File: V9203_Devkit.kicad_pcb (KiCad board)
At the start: 2 copper layers, 50 x 50 mm, 101 parts, among them J1 RJ45, J10 GS3, J2 CONN_01X16, J3 CONN_01X12, J4 Screw_Terminal_1x04, J5 GROVE-CONNECTOR-SMD-90D(4+2P-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, J6 CONN_01X09, J7 GS3, J8 GS3, J9 CONN_01X06, U1 V9203, U2 ROF-78E, Y1 Crystal_GND24

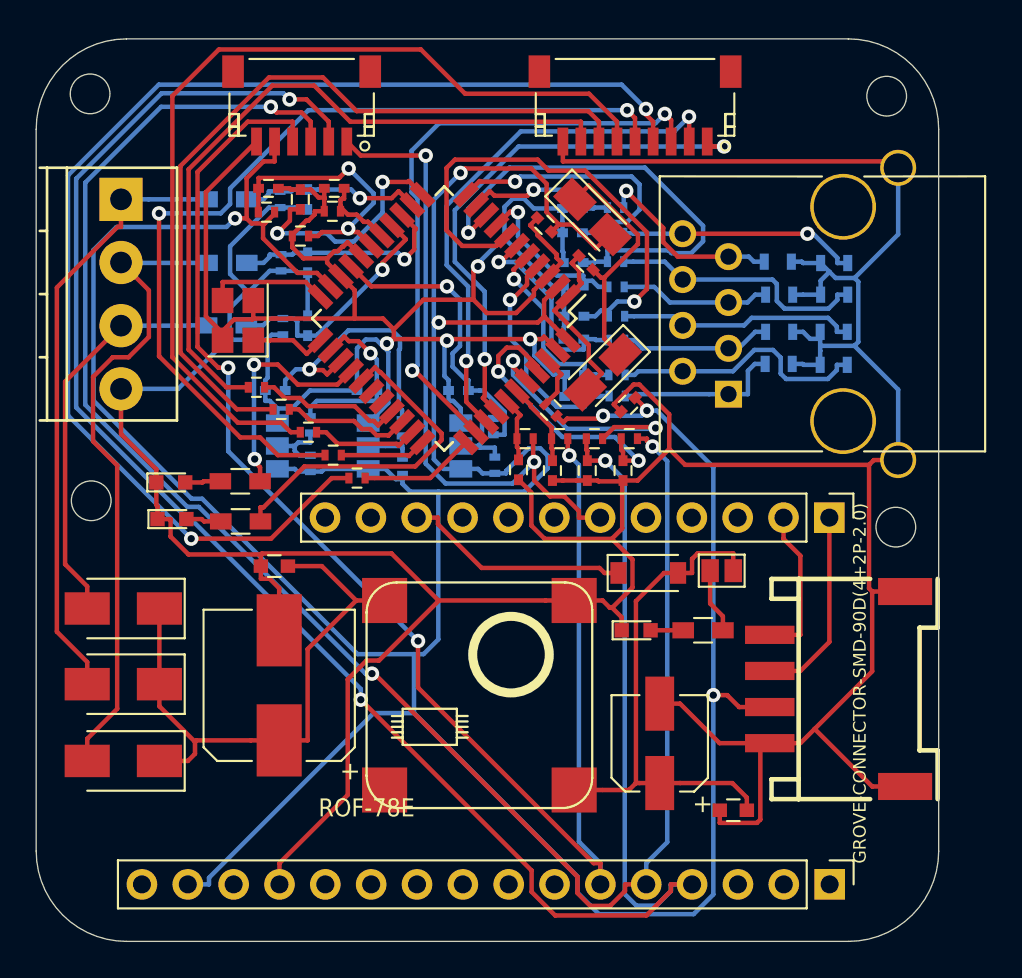
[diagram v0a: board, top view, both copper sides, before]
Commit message: With CS mux, improve silk screen in next rev
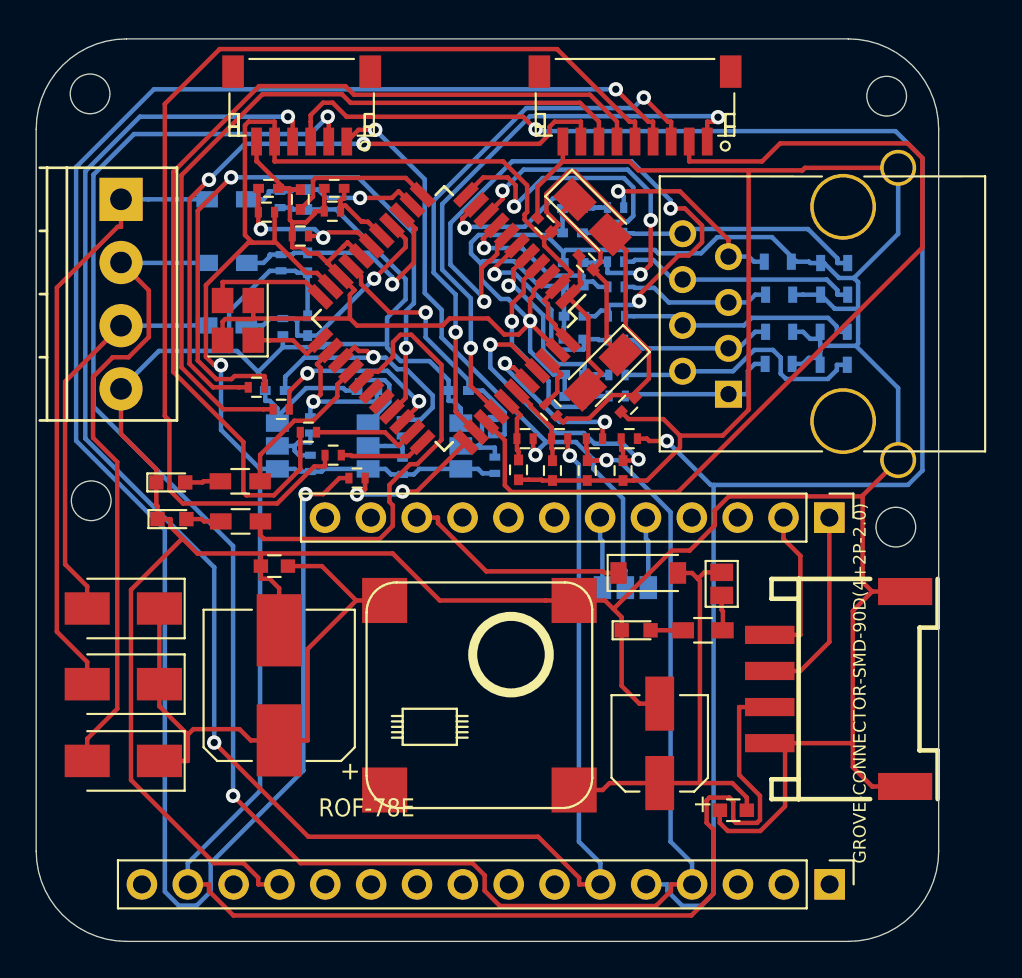
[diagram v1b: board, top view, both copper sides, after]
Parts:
- added J11: GS3, Connect:GS3, B.Cu at (142.6, 70.4)
- moved JP1 0.73 mm to (148.0, 70.2), turned to 180 degrees
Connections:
- J3 pad 6: CS -> Net-(J11-Pad1)
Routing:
- net Net-(J6-Pad4): track 69.7 -> 107.9 mm
- net +3V3: track 207.8 -> 170.5 mm, vias 6 -> 1
- net Net-(R36-Pad1): track 8.25 -> 37.5 mm, vias 0 -> 2
- net GND: track 339.4 -> 363.3 mm, vias 4 -> 1
- net Net-(J6-Pad2): track 29.8 -> 52.6 mm, vias 2 -> 0
- net SCK: track 82.2 -> 98.9 mm
- net Net-(J6-Pad5): track 50.1 -> 62.0 mm, vias 2 -> 0
- net /V9203/IBP: track 27.9 -> 36.4 mm, vias 1 -> 3
- net /V9203/ICP: track 26.5 -> 19.6 mm, vias 1 -> 3
- net Net-(R27-Pad2): track 19.0 -> 25.6 mm
- net Net-(C22-Pad2): track 15.7 -> 9.94 mm
- net /V9203/V_MISO: track 14.6 -> 9.62 mm
- net Net-(C20-Pad2): track 13.1 -> 8.40 mm, vias 2 -> 0
- net Net-(R28-Pad2): track 12.8 -> 8.82 mm, vias 2 -> 0
- net Net-(J11-Pad3): track 0.00 -> 3.93 mm
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
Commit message: Added ground plane
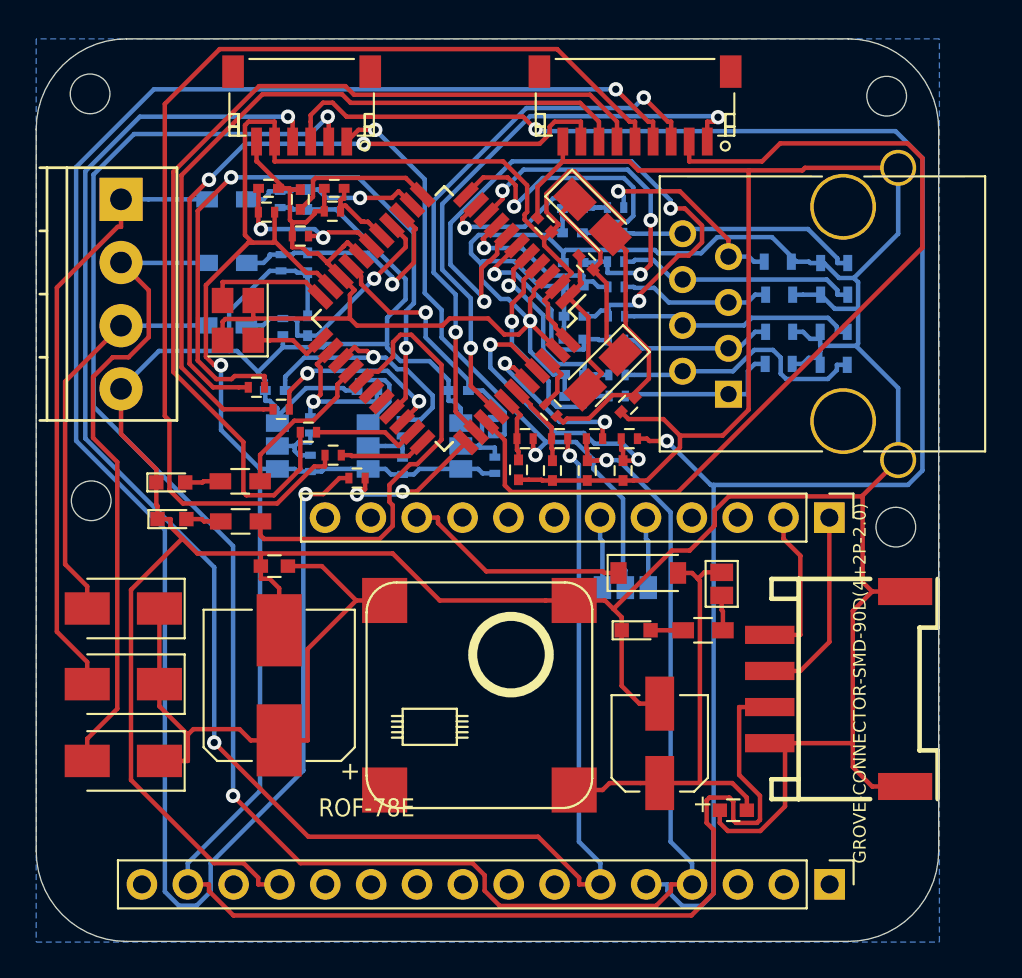
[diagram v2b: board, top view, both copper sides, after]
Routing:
- added copper zone on B.Cu, net GND
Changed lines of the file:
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@@
-(kicad_pcb (version 20170123) (host pcbnew "(2017-03-07 revision cf373e543)-makepkg")
+(kicad_pcb (version 20170123) (host pcbnew "(2017-02-28 revision fd4e2b042)-makepkg")
   (general
     (links 198)
@@
   (segment (start 143.783 67.6979) (end 143.91 67.8249) (width 0.25) (layer B.Cu) (net 93))
   (segment (start 143.783 66.5226) (end 143.783 67.6979) (width 0.25) (layer B.Cu) (net 93))
+  (zone (net 33) (net_name GND) (layer B.Cu) (hatch edge 0.508)
+    (connect_pads (clearance 0.508))
+    (min_thickness 0.254)
+    (fill yes (arc_segments 16) (thermal_gap 0.508) (thermal_bridge_width 0.508))
+    (polygon
+      (pts
+        (xy 110.001429 39.998355) (xy 110.001429 90.036355) (xy 160.039429 90.036355) (xy 160.039429 39.998355)
+      )
+    )
+  )
 )

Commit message: Added silk screen markers
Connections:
- net Net-(C28-Pad1) renamed PM1
- net Net-(C29-Pad1) renamed PM0
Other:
- board text added: "CSMUX"
- board text added: "DSLEEP"
- board text added: "PM0"
- board text added: "PM1"

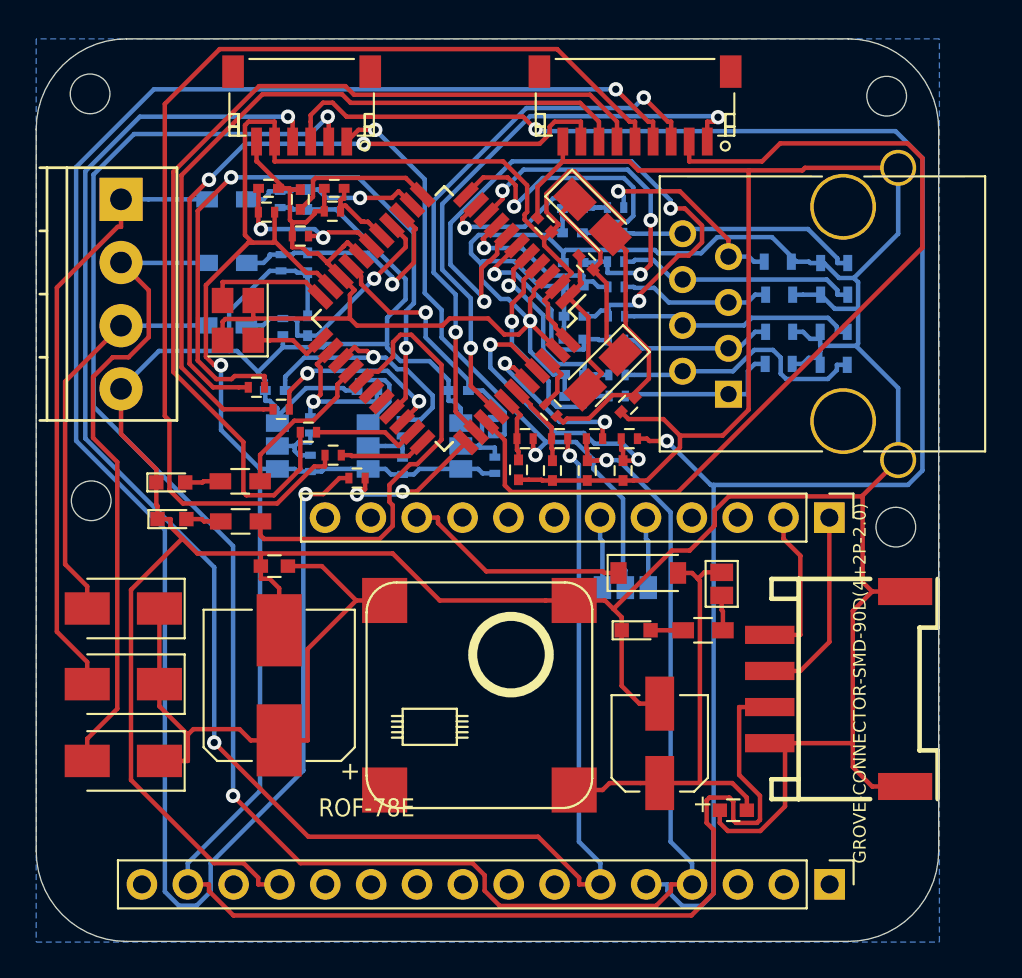
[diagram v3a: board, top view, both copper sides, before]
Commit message: Added silk screen for pins
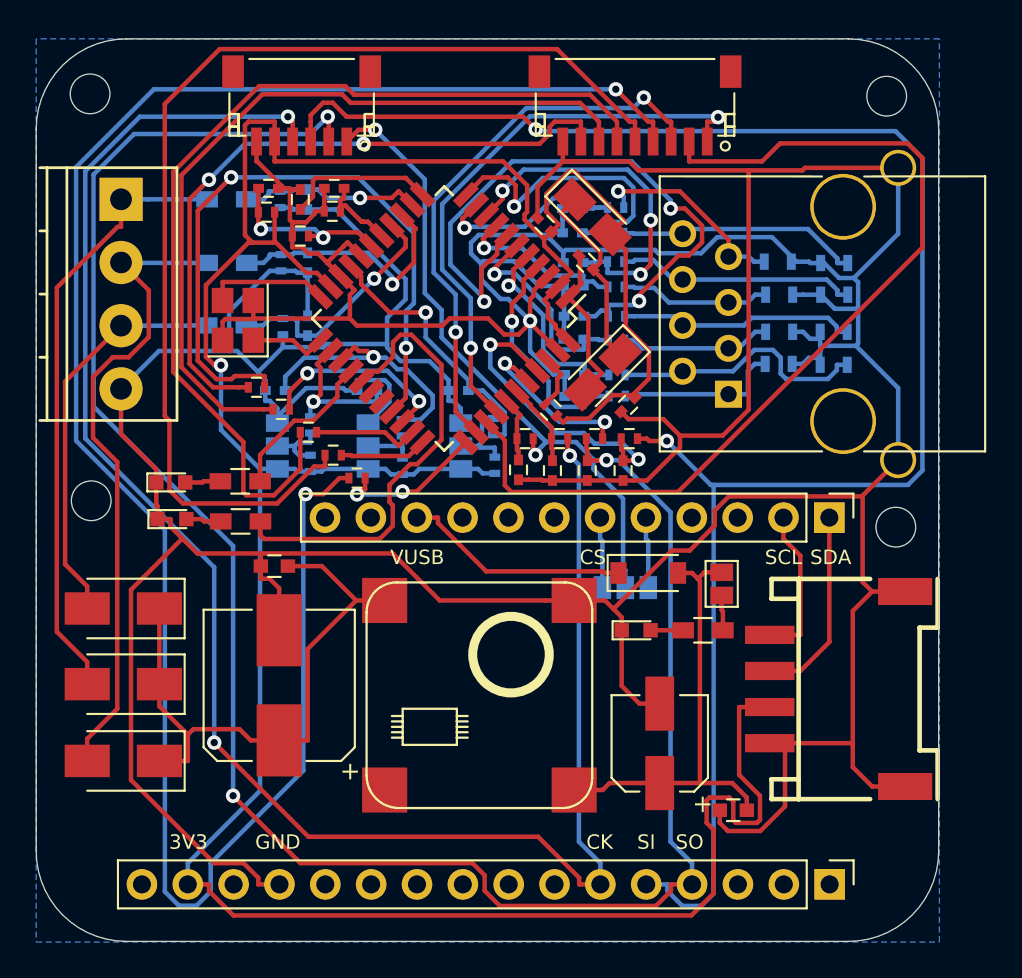
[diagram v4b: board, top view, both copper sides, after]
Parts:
- moved LOGO1 0.85 mm to (134.7, 71.2)
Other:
- board text added: "3V3"
- board text added: "CK"
- board text added: "CS"
- board text added: "GND"
- board text added: "SCK,MOSI,MISO used CS on pin 9 or 10. (0 or 15 for Huzzah)"
- board text added: "SCL"
- board text added: "SDA"
- board text added: "SI"
- board text added: "SO"
- board text added: "V9203 3-phase low voltage Energy Monitor Featherwing v1.0 02-05-2017 http://whatnick.com"
- board text added: "VUSB"
- board text removed: "V9203 3-phase low voltage Energy Monitor Featherwing http://whatnick.com"
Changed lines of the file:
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@@
-(kicad_pcb (version 20170123) (host pcbnew "(2017-02-28 revision fd4e2b042)-makepkg")
+(kicad_pcb (version 20170123) (host pcbnew "(2017-03-07 revision cf373e543)-makepkg")
   (general
     (links 198)
     (no_connects 0)
-    (area 109.994999 39.994999 160.005001 90.005001)
+    (area 107.306238 36.283 169.554549 91.950933)
     (thickness 1.6)
-    (drawings 15)
+    (drawings 25)
     (tracks 1167)
     (zones 0)
@@
     (44 Edge.Cuts user)
     (45 Margin user)
-    (46 B.CrtYd user)
-    (47 F.CrtYd user)
+    (46 B.CrtYd user hide)
+    (47 F.CrtYd user hide)
     (48 B.Fab user hide)
     (49 F.Fab user hide)
@@
   )
   (module Symbols:OSHW-Logo2_7.3x6mm_SilkScreen (layer B.Cu)
-    (at 134.829929 72.002355 180)
+    (at 134.715629 71.164155 180)
     (descr "Open Source Hardware Symbol")
     (tags "Logo Symbol OSHW")
@@
       (effects (font (size 0.001 0.001) (thickness 0.00025)))
     )
-    (fp_text value "GROVE-CONNECTOR-SMD-90D(4+2P-2.0)" (at -0.3175 -4.8895 270) (layer F.SilkS)
+    (fp_text value "GROVE-CONNECTOR-SMD-90D(4+2P-2.0)" (at 0.860755 -4.650229 270) (layer F.SilkS) hide
       (effects (font (size 0.7 0.7) (thickness 0.05)))
     )
@@
       (effects (font (size 0.001 0.001) (thickness 0.00025)))
     )
-    (fp_text value ROF-78E (at 0 0) (layer F.SilkS)
+    (fp_text value ROF-78E (at 6.182029 -1.848045) (layer F.SilkS) hide
       (effects (font (size 1 0.9) (thickness 0.05)))
     )
@@
     )
   )
+  (gr_text CS (at 140.837029 68.725755) (layer F.SilkS)
+    (effects (font (size 0.8 0.8) (thickness 0.2)))
+  )
+  (gr_text SCL (at 151.403429 68.725755) (layer F.SilkS)
+    (effects (font (size 0.8 0.8) (thickness 0.2)))
+  )
+  (gr_text SDA (at 154.019629 68.725755) (layer F.SilkS)
+    (effects (font (size 0.8 0.8) (thickness 0.2)))
+  )
+  (gr_text VUSB (at 131.108829 68.725755) (layer F.SilkS)
+    (effects (font (size 0.8 0.8) (thickness 0.2)))
+  )
+  (gr_text GND (at 123.387229 84.5) (layer F.SilkS)
+    (effects (font (size 0.8 0.8) (thickness 0.2)))
+  )
+  (gr_text 3V3 (at 118.434229 84.5) (layer F.SilkS)
+    (effects (font (size 0.8 0.8) (thickness 0.2)))
+  )
+  (gr_text CK (at 141.218029 84.5) (layer F.SilkS)
+    (effects (font (size 0.8 0.8) (thickness 0.2)))
+  )
+  (gr_text SI (at 143.8 84.5) (layer F.SilkS)
+    (effects (font (size 0.8 0.8) (thickness 0.2)))
+  )
+  (gr_text SO (at 146.2 84.5) (layer F.SilkS)
+    (effects (font (size 0.8 0.8) (thickness 0.2)))
+  )
+  (gr_text "SCK,MOSI,MISO used\nCS on pin 9 or 10. \n(0 or 15 for Huzzah)" (at 120.034429 71.214955) (layer B.SilkS)
+    (effects (font (size 0.8 0.8) (thickness 0.15)) (justify mirror))
+  )
   (gr_text DSLEEP (at 132 62.5 90) (layer B.SilkS)
     (effects (font (size 0.8 0.8) (thickness 0.2)) (justify mirror))
@@
     (effects (font (size 0.8 0.8) (thickness 0.2)) (justify mirror))
   )
-  (gr_text "V9203 3-phase low voltage\nEnergy Monitor Featherwing\nhttp://whatnick.com" (at 135.274429 80.828855) (layer B.SilkS)
+  (gr_text "V9203 3-phase low voltage\nEnergy Monitor Featherwing\nv1.0 02-05-2017\nhttp://whatnick.com" (at 134.995029 79.876355) (layer B.SilkS)
     (effects (font (size 1.5 1.5) (thickness 0.3)) (justify mirror))
   )

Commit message: Added component values from reference design
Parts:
- C1: value CP -> 220u/50V
- C10, C11, C12, C15, C17, C18, C19, C21, C28, C29, C30, C5, C6, C7, C8, C9: value C -> 100n
- C13, C14: value C -> 10u
- C16, C20, C27, C3, C4: value C -> 1u
- C2: value CP -> 100u/10V
- C22: value C -> 10n
- C23, C24, C25, C26: value C -> 1n
- J6: value CONN_01X09 -> JST9
- J9: value CONN_01X06 -> JST6
- R1, R27, R28, R29, R30, R31, R32: value R -> 1K
- R10, R11, R12, R42, R43, R44: value R -> 100K
- R13, R14, R15, R16, R2, R3, R4, R5, R6, R7, R8, R9: value R -> 100R
- R17, R18, R19, R20, R21, R22, R23, R24: value R -> 2.4R/10ppm
- R25: value R -> 75K
- R26: value R -> 43K
- R33: value R -> 10K
- R34, R35, R36, R37, R38, R39, R40, R41: value R -> 20K

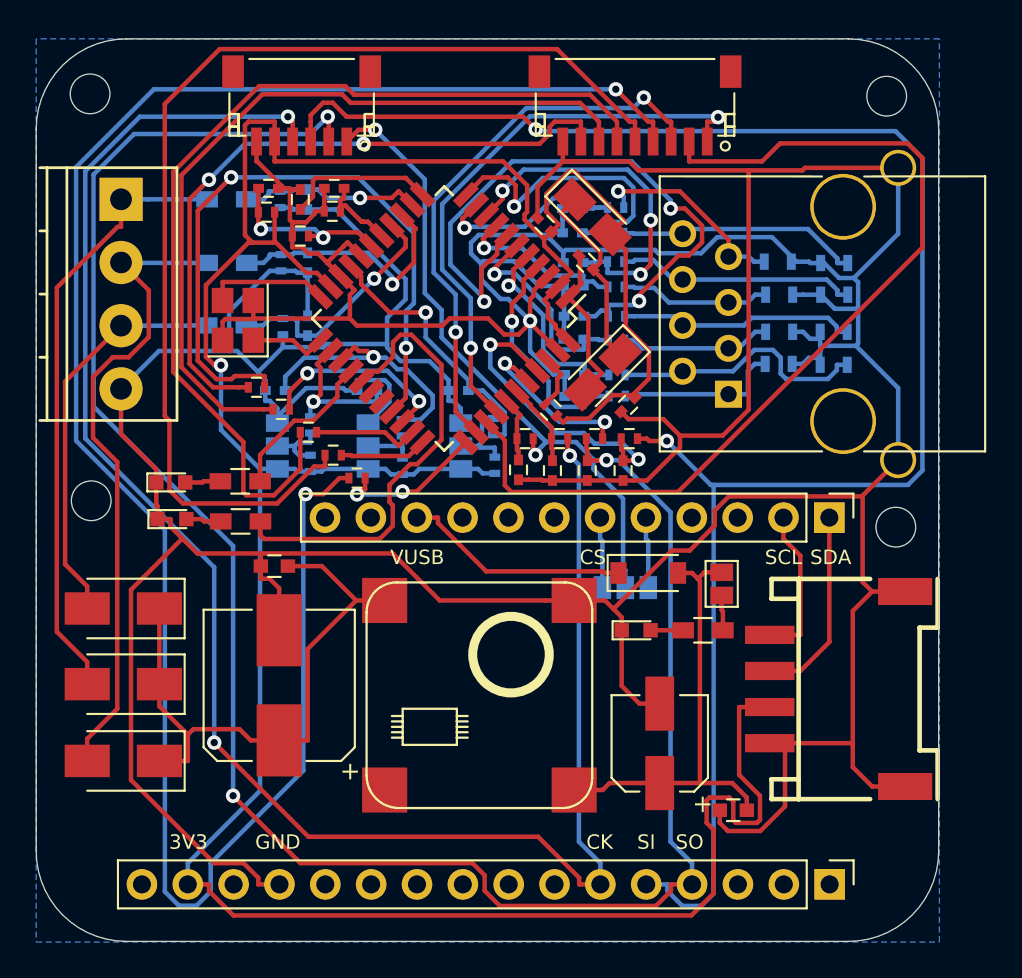
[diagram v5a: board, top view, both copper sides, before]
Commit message: Fixed a ground connection
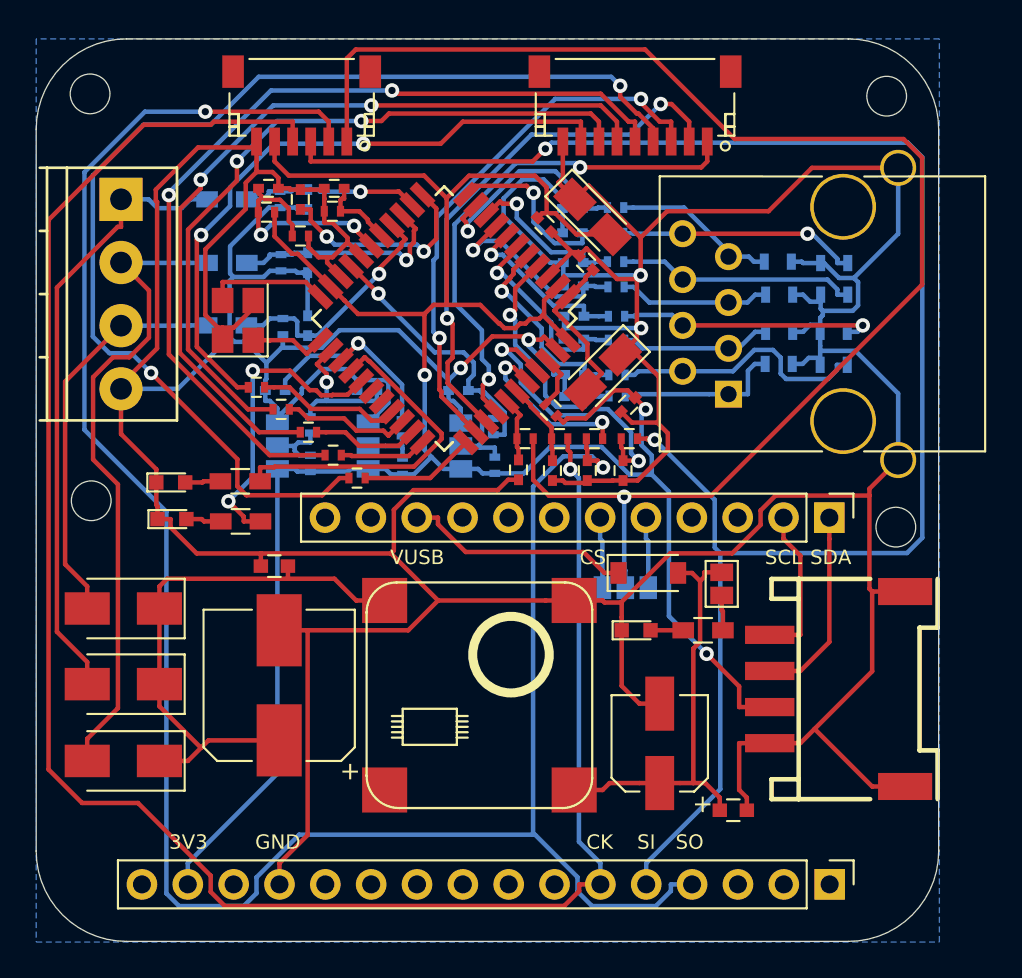
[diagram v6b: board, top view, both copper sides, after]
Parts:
- C2: value 100u/10V -> 100u/16V
- C3: value 1u -> 1u/16V
- C4: value 1u -> 1u/50V
- turned C15 to 315 degrees
- turned C27 to 135 degrees
- turned C3 to 0 degrees
- turned R26 to 180 degrees
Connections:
- C13 pad 1: Net-(C13-Pad1) -> GND
- C14 pad 1: Net-(C13-Pad1) -> GND
- C15 pad 1: Net-(C13-Pad1) -> GND
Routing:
- net CS: track 35.8 -> 80.4 mm, vias 2 -> 1
- net Net-(J6-Pad4): track 107.9 -> 63.6 mm
- net +3V3: track 170.5 -> 135.7 mm, vias 1 -> 3
- net Net-(R36-Pad1): track 37.5 -> 8.02 mm, vias 2 -> 0
- net /V9203/IBP: track 36.4 -> 9.67 mm, vias 3 -> 1
- net Net-(J6-Pad2): track 52.6 -> 30.0 mm, vias 0 -> 2
- net Net-(J6-Pad5): track 62.0 -> 49.9 mm, vias 0 -> 2
- net Net-(C13-Pad1): track 10.6 -> 0.00 mm
- net /V9203/ICP: track 19.6 -> 9.25 mm, vias 3 -> 1
- net Net-(R28-Pad2): track 8.82 -> 18.9 mm
- net SCK: track 98.9 -> 107.7 mm, vias 3 -> 1
- net Net-(J6-Pad6): track 53.7 -> 44.9 mm, vias 0 -> 2
- net Net-(R27-Pad2): track 25.6 -> 17.1 mm, vias 0 -> 2
- net MISO: track 110.7 -> 118.9 mm, vias 3 -> 2
- net GND: track 363.3 -> 356.7 mm, vias 1 -> 4
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
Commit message: Bump version
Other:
- board text added: "V9203 3-phase low voltage Energy Monitor Featherwing v1.1 05-06-2017 http://whatnick.com"
- board text removed: "V9203 3-phase low voltage Energy Monitor Featherwing v1.0 02-05-2017 http://whatnick.com"
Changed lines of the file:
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@@
     (effects (font (size 0.8 0.8) (thickness 0.2)) (justify mirror))
   )
-  (gr_text "V9203 3-phase low voltage\nEnergy Monitor Featherwing\nv1.0 02-05-2017\nhttp://whatnick.com" (at 134.995029 79.876355) (layer B.SilkS)
+  (gr_text "V9203 3-phase low voltage\nEnergy Monitor Featherwing\nv1.1 05-06-2017\nhttp://whatnick.com" (at 134.995029 79.876355) (layer B.SilkS)
     (effects (font (size 1.5 1.5) (thickness 0.3)) (justify mirror))
   )
